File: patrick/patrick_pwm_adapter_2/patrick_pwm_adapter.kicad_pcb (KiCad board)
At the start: 2 copper layers, 34.2 x 23.9 mm, 10 parts, among them IC1 IS32FL3237-TQLA3, J1 Conn_01x13, J2 Conn_01x13

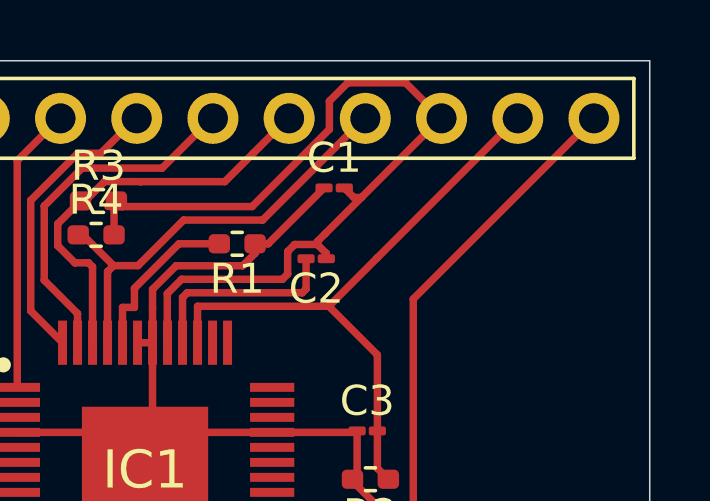
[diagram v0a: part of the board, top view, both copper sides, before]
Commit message: slight change to correct problem with IS32 breakout board
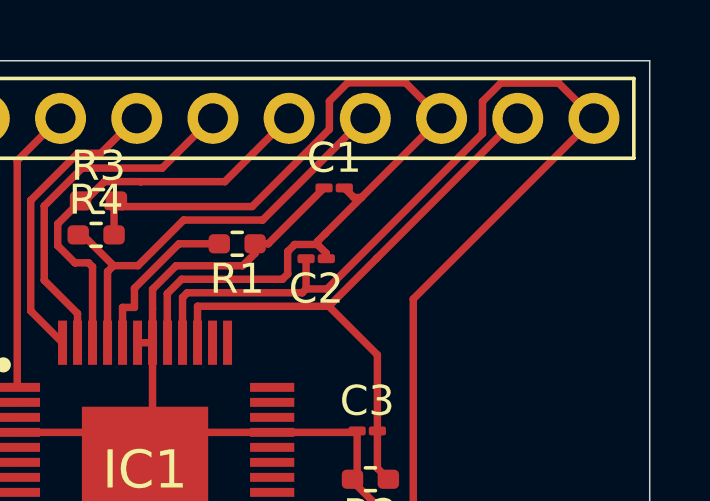
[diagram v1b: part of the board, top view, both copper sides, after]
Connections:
- net Net-(IC1-Pad45) renamed /SDA
- net Net-(IC1-Pad46) renamed /SCL
- C2 pad 2: Net-(C2-Pad2) -> GND
- IC1 pad 40: Net-(C2-Pad2) -> GND
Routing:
- net GND: track 64.7 -> 85.0 mm
- net Net-(C2-Pad2): track 6.75 -> 0.00 mm
